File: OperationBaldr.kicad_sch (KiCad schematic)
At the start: 20 parts, among them J1 Conn_01x10_Pin, J2 Conn_01x04_Pin, U4 ULN2003A, U5 ULN2003A, U6 74HC595, U7 74HC595, U8 74HC595, U9 ULN2003A

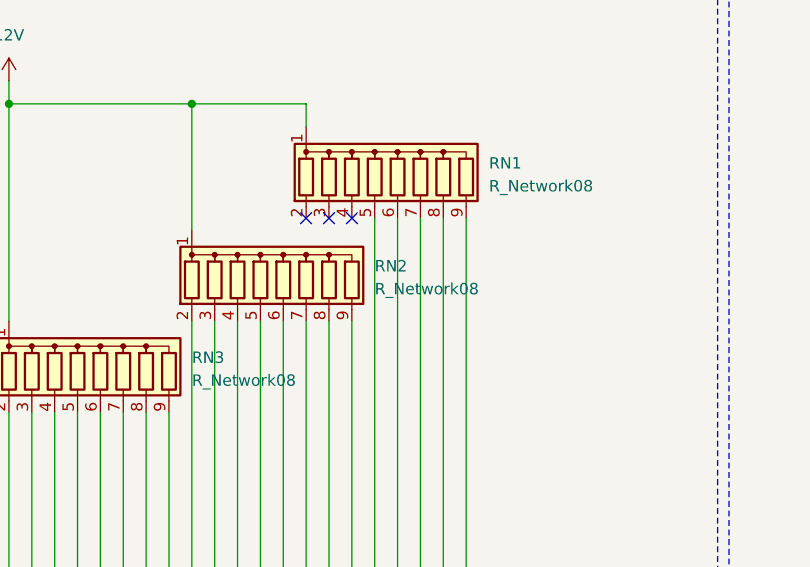
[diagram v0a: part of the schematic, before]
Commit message: Added cad directory
Added cad directory with casing step file. Also made a minor
schematic revision (adding values to the resistor networks).
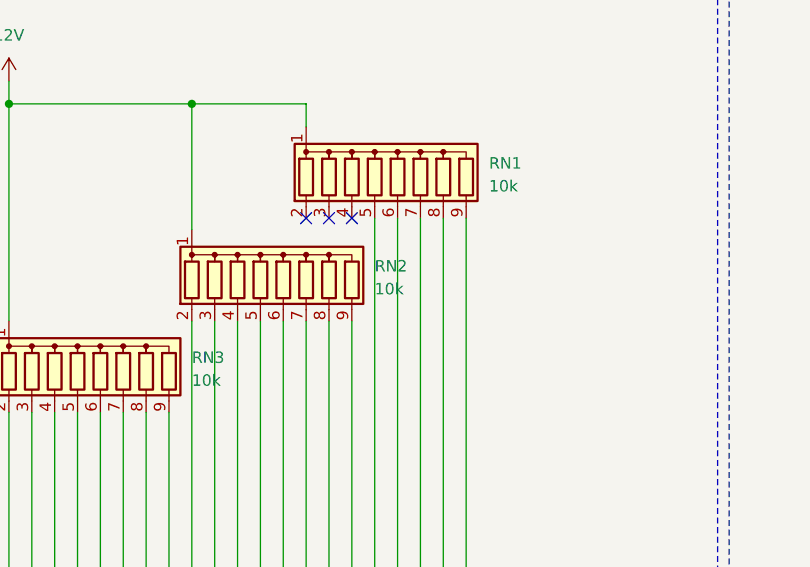
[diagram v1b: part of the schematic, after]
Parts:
- RN1, RN2, RN3: value R_Network08 -> 10k
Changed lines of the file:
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@@
 	(title_block
 		(title "Baldr Schematic")
-		(date "2024-06-18")
-		(rev "0.1.0")
+		(date "2024-07-05")
+		(rev "0.1.1")
 	)
 	(junction
@@
 			)
 		)
-		(property "Value" "R_Network08"
+		(property "Value" "10k"
 			(at 167.64 194.5639 0)
 			(effects
@@
 			)
 		)
-		(property "Value" "R_Network08"
+		(property "Value" "10k"
 			(at 134.62 216.1539 0)
 			(effects
@@
 			)
 		)
-		(property "Value" "R_Network08"
+		(property "Value" "10k"
 			(at 154.94 205.9939 0)
 			(effects
